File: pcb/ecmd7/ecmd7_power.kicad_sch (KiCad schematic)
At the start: 70 parts, among them Q10 BSC098N10NS5, Q7 BSC098N10NS5, Q8 BSC098N10NS5, Q9 BSC098N10NS5, U14 LM5118MH, U3 LM5118MH, U6 TLV71318PDBV, U9 LT1616ES6#TRPBF

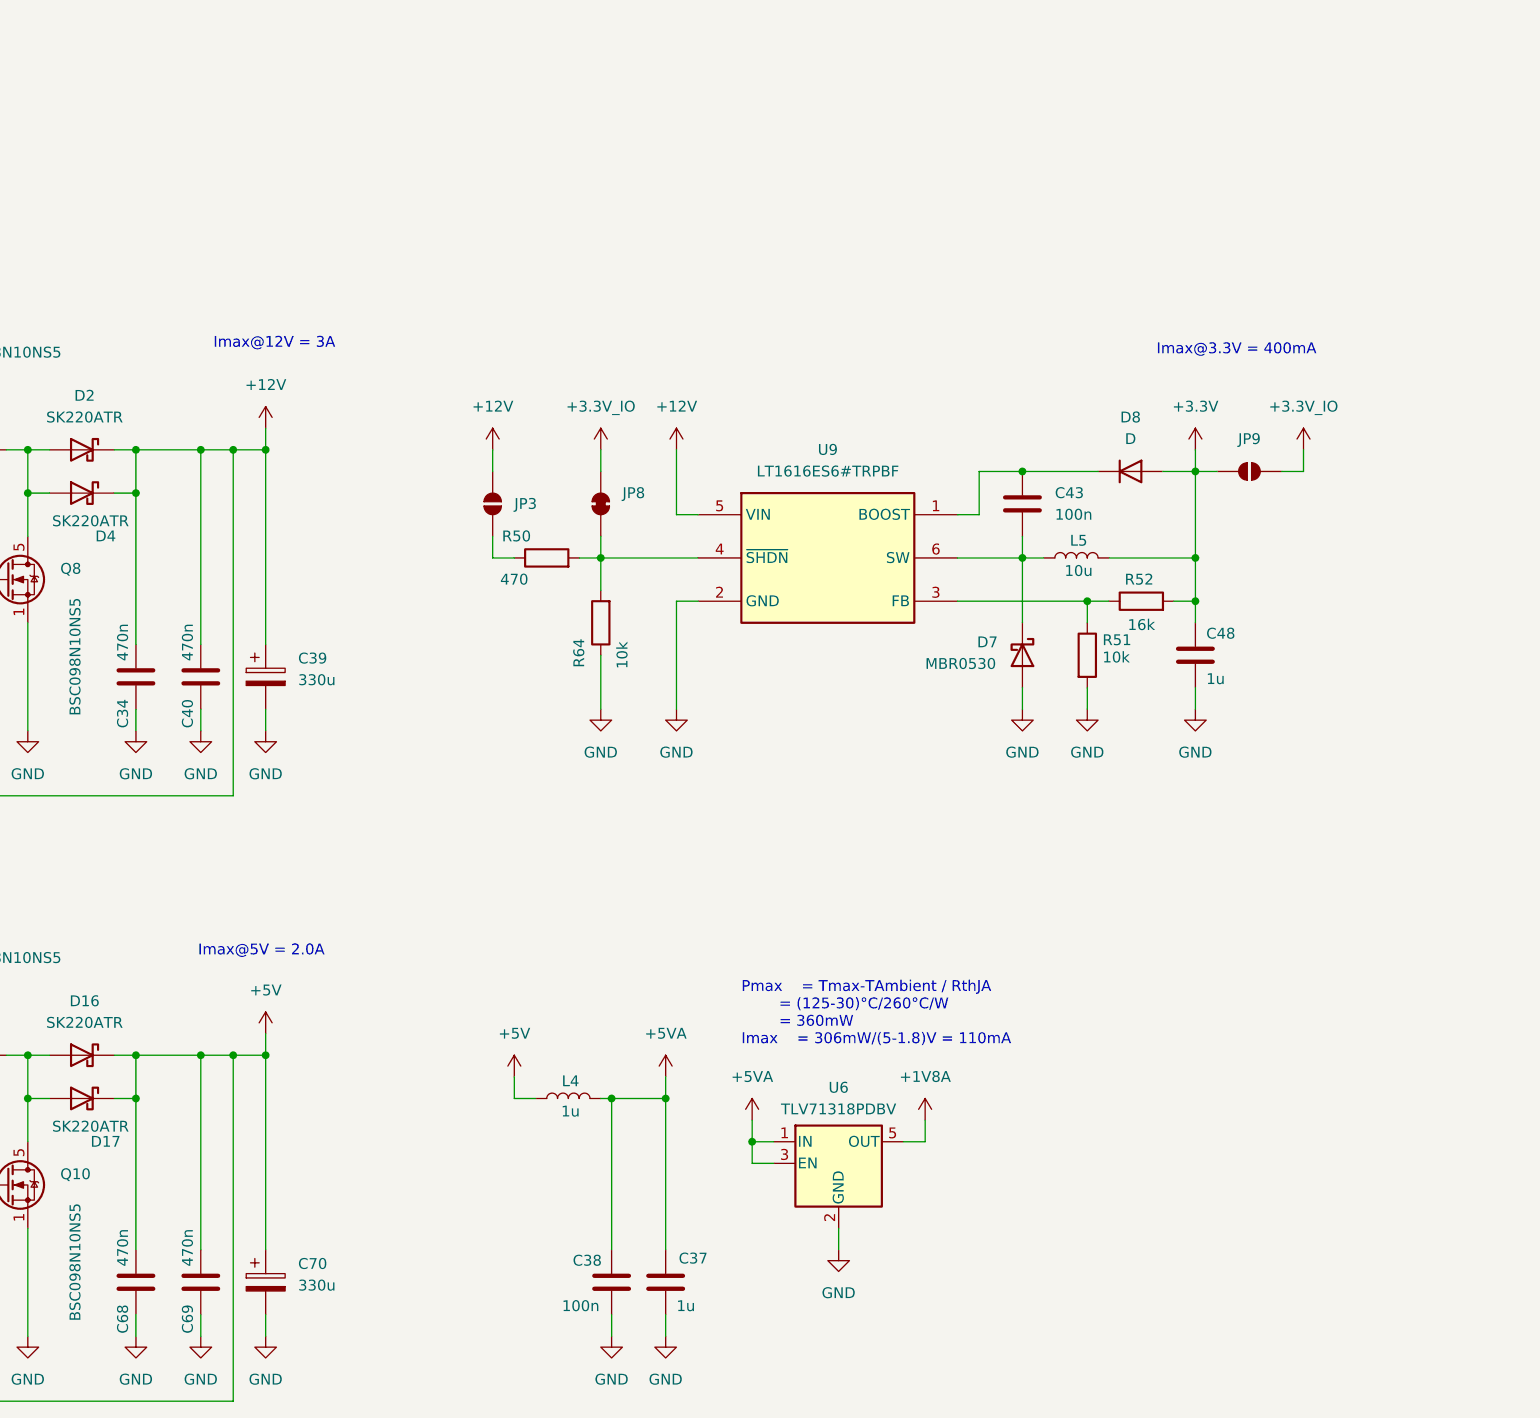
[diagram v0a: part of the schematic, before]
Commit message: WIP: Update symbols, fix ERC errors
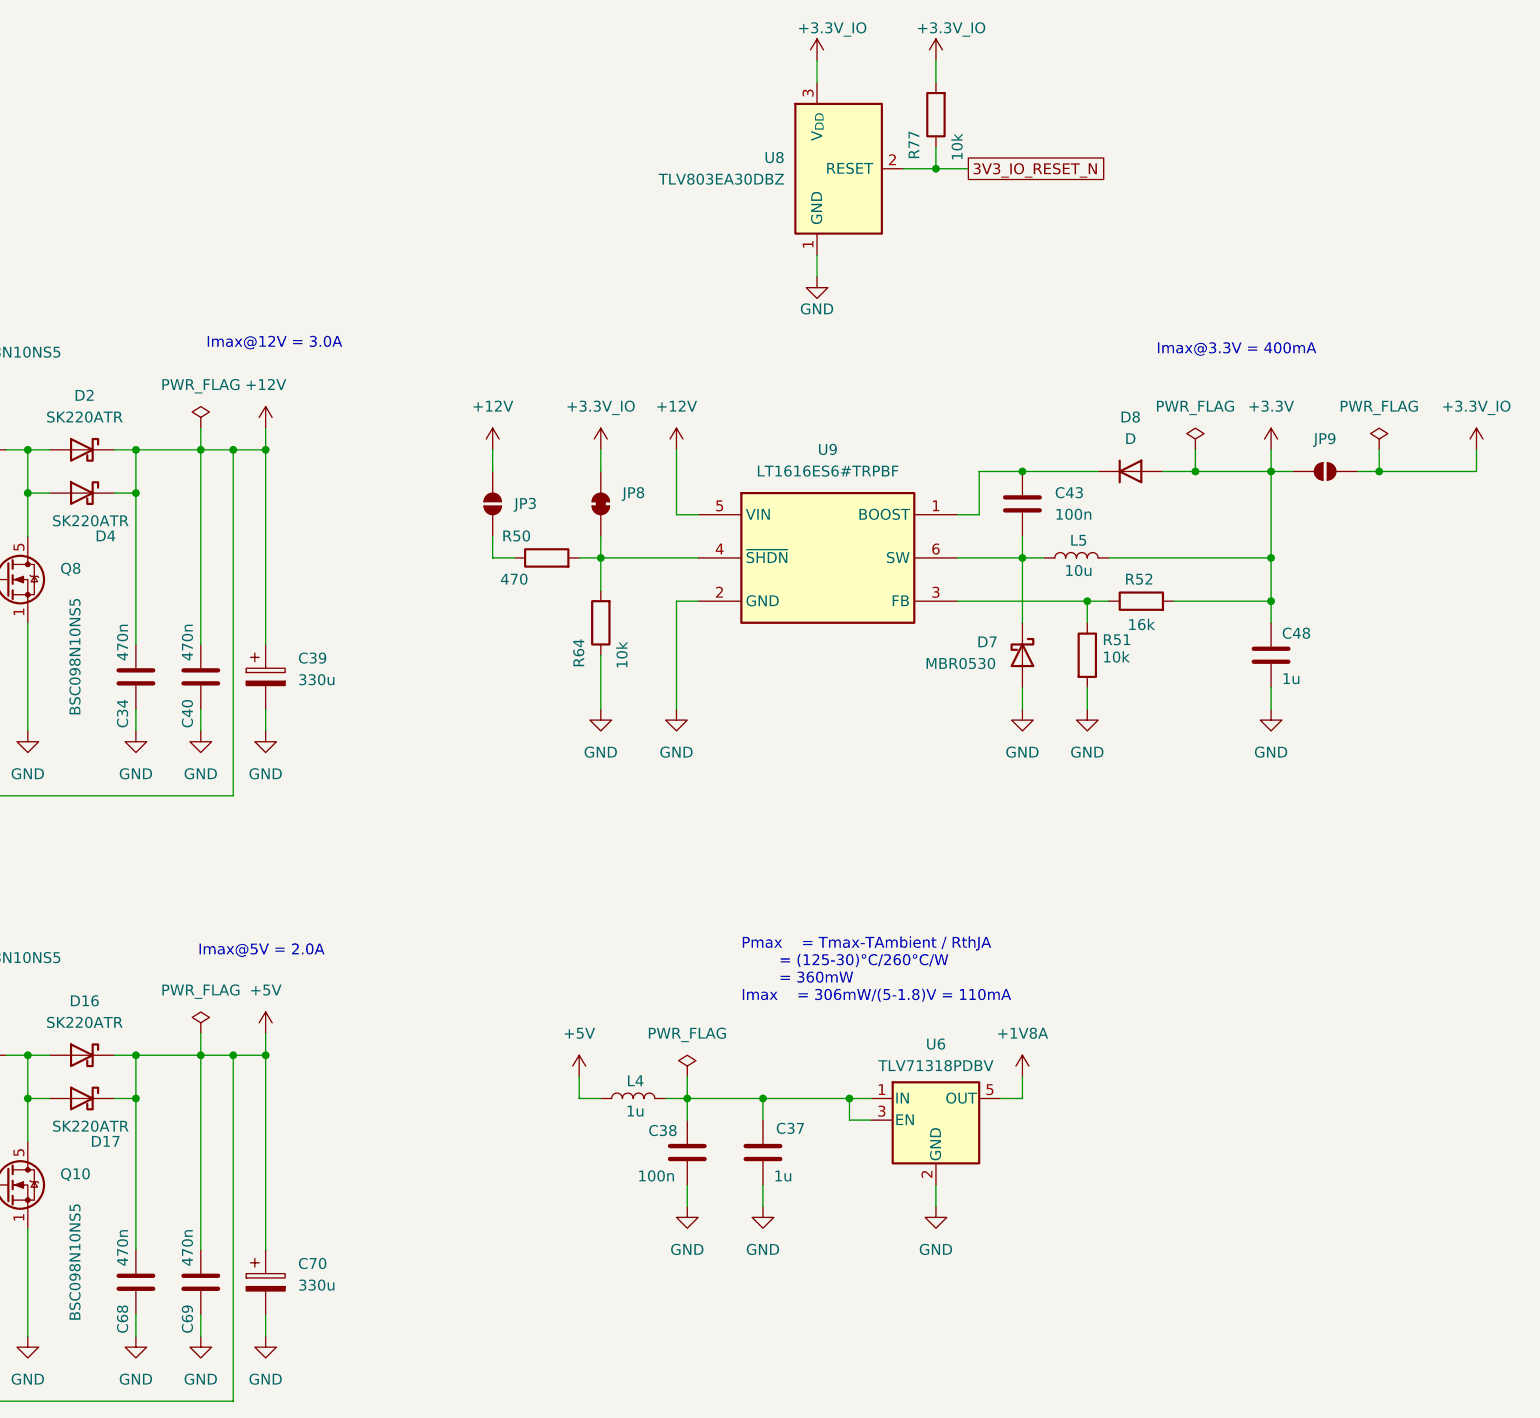
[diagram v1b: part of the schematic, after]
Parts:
- added R77: 10k, Resistor_SMD:R_0805_2012Metric, symbol Device:R
- added U8: TLV803EA30DBZ, Package_TO_SOT_SMD:SOT-23, symbol Power_Supervisor:TLV810EA29DBZ
- U9: symbol ssta_symbols:LT1616ES6#TRPBF -> SSTA:LT1616ES6#TRPBF
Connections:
- net +3.3V_IO: now also R77.2, U8.3 (V_{DD})
- net GND: now also U8.1 (GND)
- net +5VA: no longer names the net of C37.1, C38.1, L4.2, U6.1 (IN), U6.3 (EN)
- new net 3V3_IO_RESET_N: R77.1, U8.2 (RESET)
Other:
- note added: "Imax@12V = 3.0A"
- note removed: "Imax@12V = 3A"
- moved on the sheet: C37, C38, C48, JP9, L4, U6

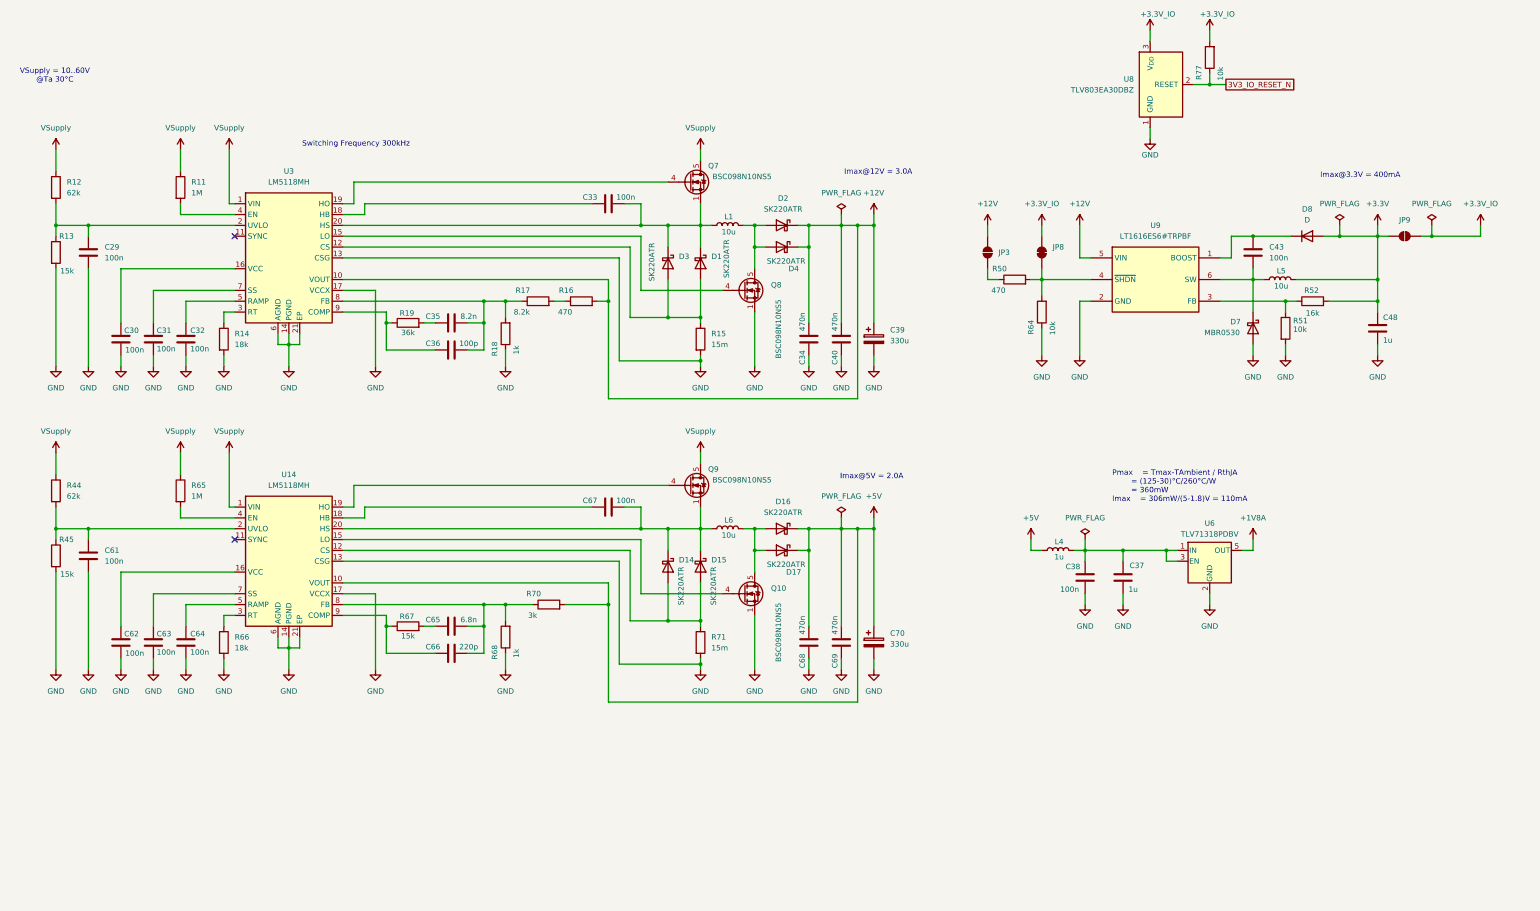
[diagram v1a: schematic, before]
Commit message: WIP: Partial routing
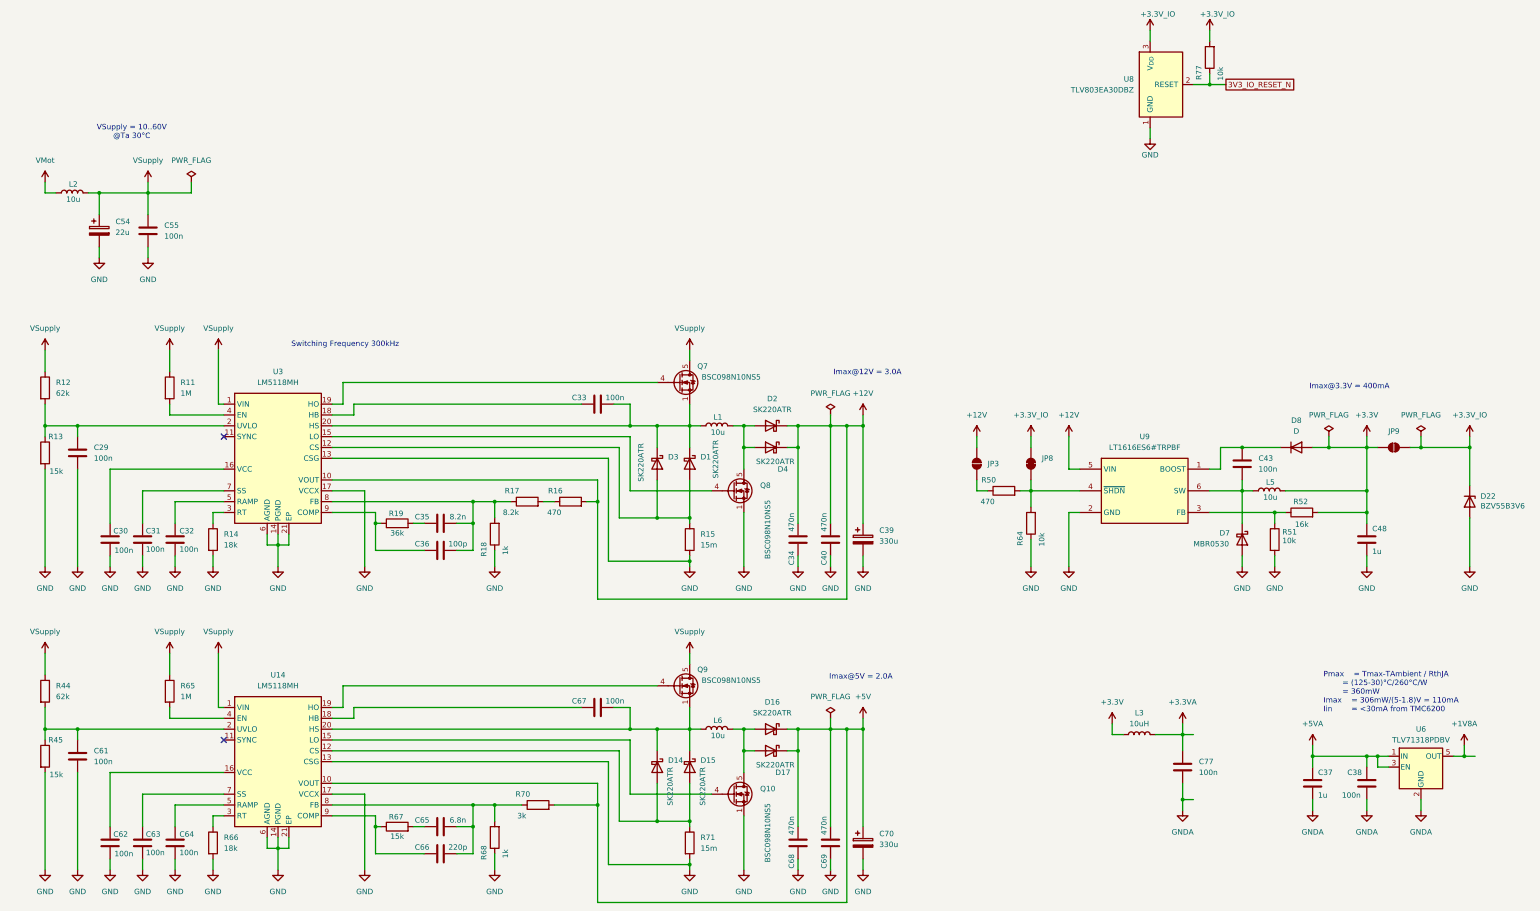
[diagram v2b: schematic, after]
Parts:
- removed L4: 1u, Inductor_SMD:L_0805_2012Metric, symbol Device:L
- added C54: 22u, Capacitor_SMD:CP_Elec_6.3x9.9, symbol Device:C_Polarized
- added C55, C77: 100n, Capacitor_SMD:C_0805_2012Metric, symbol Device:C
- added D22: BZV55B3V6, Diode_SMD:D_MiniMELF, symbol Diode:BZV55B3V6
- added L2: 10u, Inductor_SMD:L_TechFuse_SL0530, symbol Device:L
- added L3: 10uH, Inductor_SMD:L_0805_2012Metric, symbol Device:L
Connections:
- net +3.3V: now also L3.1
- net +3.3V_IO: now also D22.1 (K)
- net GND: now also C54.2, C55.2, D22.2 (A); no longer C37.2, C38.2, U6.2 (GND)
- net VSupply: now also C54.1, C55.1, L2.2
- net +5VA: now reaches C37.1, C38.1, U6.1 (IN), U6.3 (EN)
- new net +3.3VA: C77.1, L3.2
- new net GNDA: C37.2, C38.2, C77.2, U6.2 (GND)
- new net VMot: L2.1
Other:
- note added: "Pmax = Tmax-TAmbient / RthJA = (125-30)°C/260°C/W = 360mW Imax = 306mW/(5-1.8)V = 110mA Iin = <30mA from TMC6200"
- note removed: "Pmax = Tmax-TAmbient / RthJA = (125-30)°C/260°C/W = 360mW Imax = 306mW/(5-1.8)V = 110mA"
- moved on the sheet: C29, C30, C31, C32, C33, C34, C35, C36, C37, C38, C39, C40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

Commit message: WIP: advnced  routing
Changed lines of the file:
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@@
 	)
 	(junction
-		(at 317.5 217.17)
-		(diameter 0)
-		(color 0 0 0 0)
-	)
-	(junction
 		(at 180.34 218.44)
 		(diameter 0)
@@
 	)
 	(junction
-		(at 383.54 207.01)
-		(diameter 0)
-		(color 0 0 0 0)
-	)
-	(junction
 		(at 58.42 200.66)
 		(diameter 0)
@@
 	(wire
 		(pts
+			(xy 317.5 201.93) (xy 327.66 201.93)
+		)
+		(stroke
+			(width 0)
+			(type default)
+		)
+	)
+	(wire
+		(pts
 			(xy 66.04 231.14) (xy 66.04 233.68)
 		)
@@
 	(wire
 		(pts
-			(xy 317.5 213.36) (xy 317.5 217.17)
+			(xy 317.5 213.36) (xy 317.5 219.71)
 		)
 		(stroke
@@
 	(wire
 		(pts
-			(xy 317.5 217.17) (xy 320.04 217.17)
-		)
-		(stroke
-			(width 0)
-			(type default)
-		)
-	)
-	(wire
-		(pts
 			(xy 227.33 129.54) (xy 234.95 129.54)
 		)
@@
 	(wire
 		(pts
-			(xy 317.5 217.17) (xy 317.5 219.71)
-		)
-		(stroke
-			(width 0)
-			(type default)
-		)
-	)
-	(wire
-		(pts
 			(xy 290.83 149.86) (xy 290.83 162.56)
 		)
@@
 	(wire
 		(pts
+			(xy 327.66 201.93) (xy 327.66 199.39)
+		)
+		(stroke
+			(width 0)
+			(type default)
+		)
+	)
+	(wire
+		(pts
 			(xy 214.63 134.62) (xy 214.63 139.7)
 		)
@@
 	(wire
 		(pts
-			(xy 383.54 207.01) (xy 386.08 207.01)
-		)
-		(stroke
-			(width 0)
-			(type default)
-		)
-	)
-	(wire
-		(pts
 			(xy 227.33 200.66) (xy 234.95 200.66)
 		)
@@
 	(wire
 		(pts
-			(xy 320.04 201.93) (xy 317.5 201.93)
-		)
-		(stroke
-			(width 0)
-			(type default)
-		)
-	)
-	(wire
-		(pts
 			(xy 128.27 229.87) (xy 128.27 223.52)
 		)
@@
 		)
 	)
-	(netclass_flag ""
-		(length 2.54)
-		(shape round)
-		(at 386.08 207.01 270)
-		(effects
-			(font
-				(size 1.27 1.27)
-			)
-			(justify right bottom)
-		)
-		(property "Netclass" "Analog"
-			(at 390.144 207.01 0)
-			(effects
-				(font
-					(size 1.27 1.27)
-				)
-				(justify left)
+	(rule_area
+		(polyline
+			(pts
+				(xy 308.61 184.15) (xy 392.43 184.15) (xy 392.43 229.87) (xy 308.61 229.87)
+			)
+			(stroke
+				(width 0)
+				(type dash)
 			)
-		)
-		(property "Component Class" ""
-			(at -38.1 44.45 0)
-			(effects
-				(font
-					(size 1.27 1.27)
-					(italic yes)
-				)
+			(fill
+				(type none)
 			)
 		)
@@
 		(length 2.54)
 		(shape round)
-		(at 320.04 217.17 270)
-		(effects
-			(font
-				(size 1.27 1.27)
-			)
-			(justify right bottom)
-		)
-		(property "Netclass" "Analog"
-			(at 324.104 217.17 0)
-			(effects
-				(font
-					(size 1.27 1.27)
-				)
-				(justify left)
-			)
-		)
-		(property "Component Class" ""
-			(at -104.14 54.61 0)
-			(effects
-				(font
-					(size 1.27 1.27)
-					(italic yes)
-				)
-			)
-		)
-	)
-	(netclass_flag ""
-		(length 2.54)
-		(shape round)
-		(at 320.04 201.93 270)
+		(at 340.36 184.15 0)
+		(fields_autoplaced yes)
 		(effects
 			(font
 				(size 1.27 1.27)
 			)
-			(justify right bottom)
+			(justify left bottom)
 		)
 		(property "Netclass" "Analog"
-			(at 324.104 201.93 0)
+			(at 341.0585 181.61 0)
 			(effects
 				(font
@@
 		)
 		(property "Component Class" ""
-			(at -104.14 39.37 0)
+			(at -144.78 -6.35 0)
 			(effects
 				(font
@@
 					(unit 1)
 				)
+			)
+		)
+	)
+	(symbol
+		(lib_id "power:PWR_FLAG")
+		(at 327.66 199.39 0)
+		(unit 1)
+		(exclude_from_sim no)
+		(in_bom yes)
+		(on_board yes)
+		(dnp no)
+		(fields_autoplaced yes)
+		(property "Reference" "#FLG011"
+			(at 327.66 197.485 0)
+			(effects
+				(font
+					(size 1.27 1.27)
+				)
+				(hide yes)
+			)
+		)
+		(property "Value" "PWR_FLAG"
+			(at 327.66 194.31 0)
+			(effects
+				(font
+					(size 1.27 1.27)
+				)
+			)
+		)
+		(property "Footprint" ""
+			(at 327.66 199.39 0)
+			(effects
+				(font
+					(size 1.27 1.27)
+				)
+				(hide yes)
+			)
+		)
+		(property "Datasheet" "~"
+			(at 327.66 199.39 0)
+			(effects
+				(font
+					(size 1.27 1.27)
+				)
+				(hide yes)
+			)
+		)
+		(property "Description" "Special symbol for telling ERC where power comes from"
+			(at 327.66 199.39 0)
+			(effects
+				(font
+					(size 1.27 1.27)
+				)
+				(hide yes)
+			)
+		)
+		(pin "1"
+		)
+		(instances
+			(project "ecmd7"
+				(path "/e730e626-b0ba-4026-9c00-58e2460691fe/da8b1e93-5d51-40db-83cb-e313b5e0b1d9"
+					(reference "#FLG011")
+					(unit 1)
+				)
